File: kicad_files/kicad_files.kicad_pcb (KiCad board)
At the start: 2 copper layers, 150 x 100 mm, 68 parts, among them J1 Battery Connection, J2 Servo Connection, J3 DC Motor Connection, J4 Washout Ultrasonic Sensor Con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, J5 Water Sensor Connection, J6 Servo Connection, J7 Larvicide Level Ultrasonic Se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, Q1 FS8205A, Q2 NPN, Q3 NMOS, Q4 NMOS, Q5 NPN, Q7 NMOS, U1 BQ27441DRZR-G1A, U2 DW01A, U3 TPS61023DRLR, U4 LM311, U5 LMC555CMMX_NOPB, U6 LMC555CMMX_NOPB

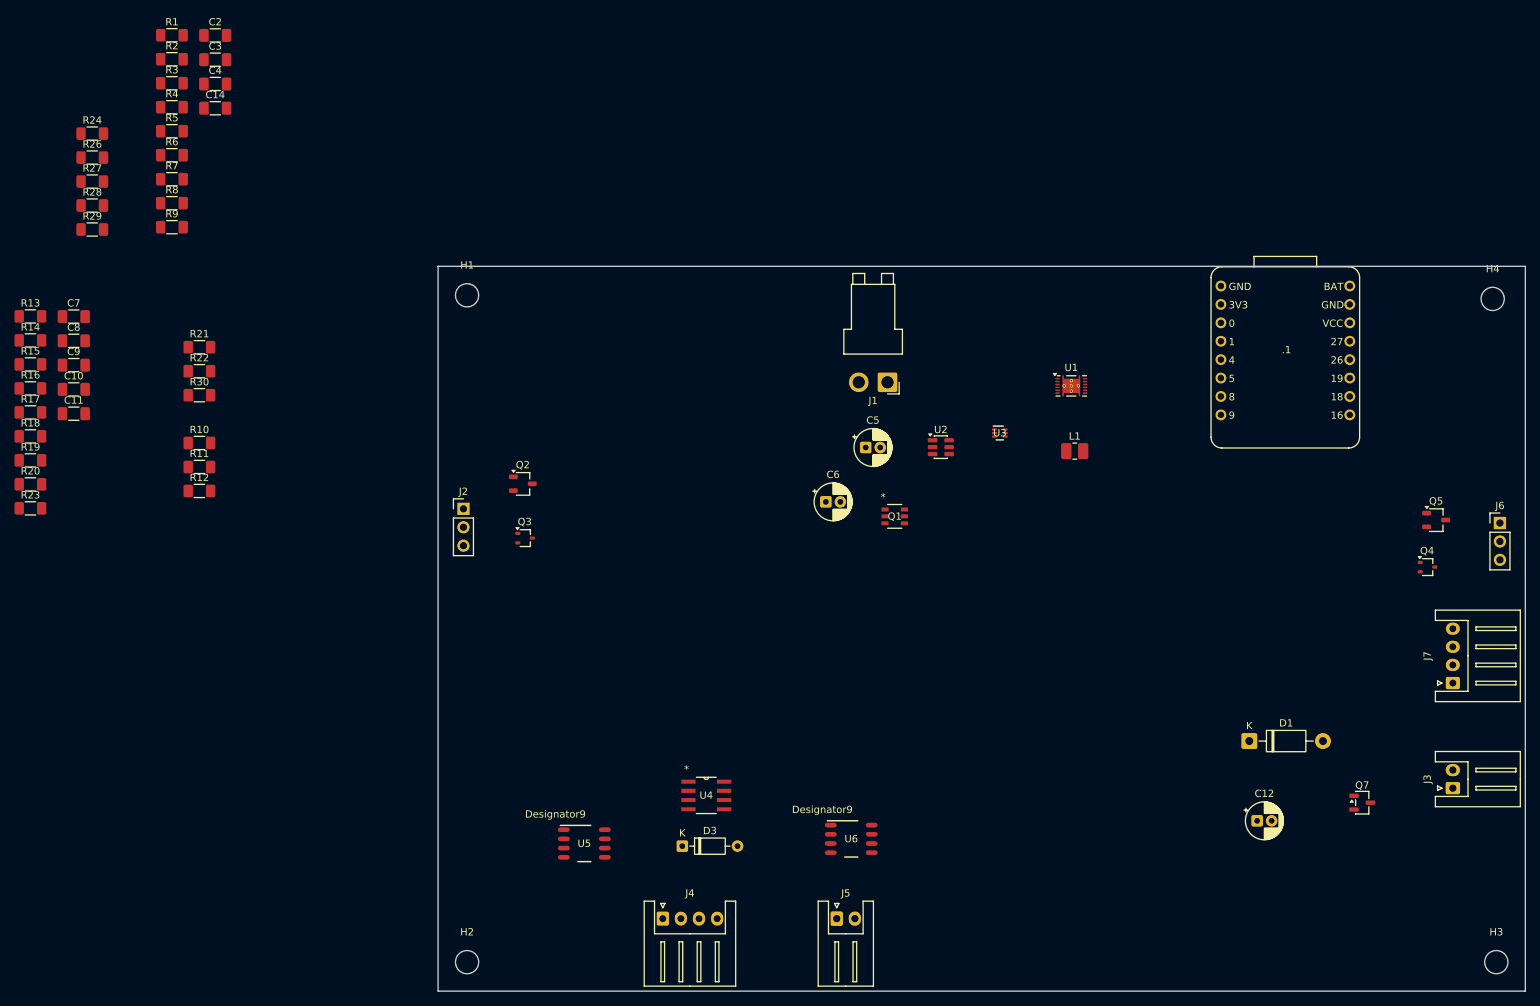
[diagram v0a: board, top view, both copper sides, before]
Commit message: Housing and Dispensing Subsystem Models
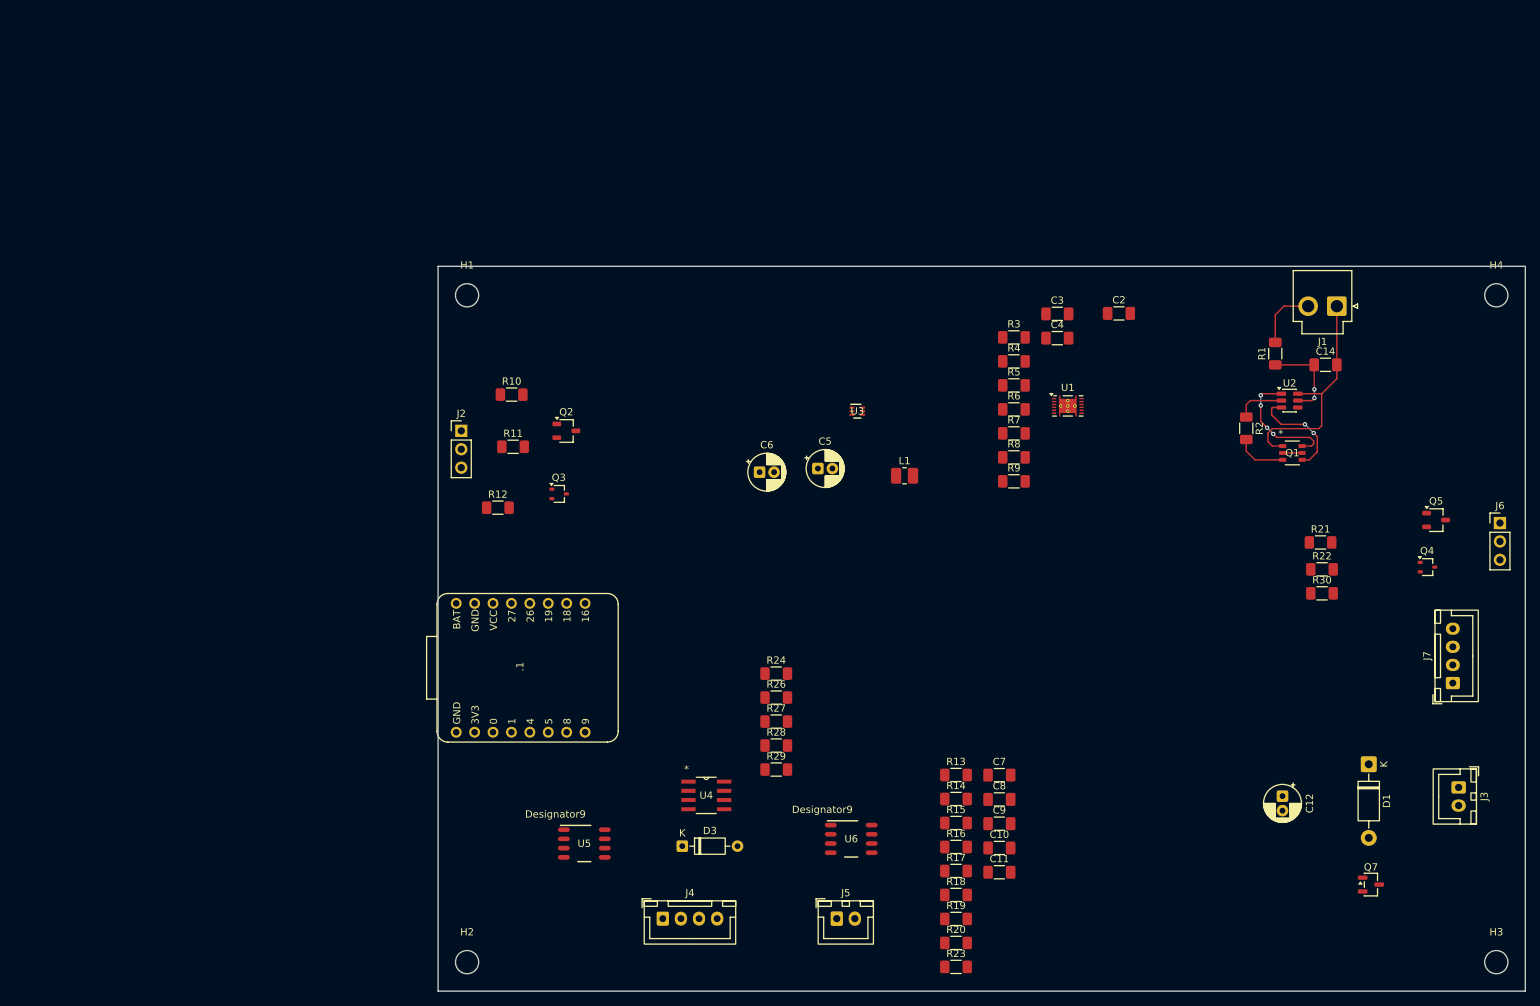
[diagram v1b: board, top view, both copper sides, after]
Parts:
- J1: footprint Connector_JST:JST_VH_B2PS-VH_1x02_P3.96mm_Horizontal -> Connector_JST:JST_VH_B2P-VH_1x02_P3.96mm_Vertical
- J3, J5: footprint Connector_JST:JST_XH_S2B-XH-A_1x02_P2.50mm_Horizontal -> Connector_JST:JST_XH_B2B-XH-A_1x02_P2.50mm_Vertical
- J4, J7: footprint Connector_JST:JST_XH_S4B-XH-A_1x04_P2.50mm_Horizontal -> Connector_JST:JST_XH_B4B-XH-A_1x04_P2.50mm_Vertical
- moved R1 158.4 mm to (215.5, 62.0), turned to 90 degrees
- moved R22 157.3 mm to (221.9, 91.8)
- moved R30 157.3 mm to (221.9, 95.1)
- moved C14 157.2 mm to (222.4, 63.6)
- moved R21 157.0 mm to (221.8, 88.1)
- moved R2 156.7 mm to (211.5, 72.3), turned to -90 degrees
- moved R13 142.5 mm to (171.5, 120.2)
- moved R14 142.5 mm to (171.5, 123.5)
- moved R15 142.5 mm to (171.5, 126.8)
- moved R16 142.5 mm to (171.5, 130.1)
- moved R17 142.5 mm to (171.5, 133.4)
- moved R18 142.5 mm to (171.5, 136.7)
- moved R19 142.5 mm to (171.5, 140.0)
- moved R20 142.5 mm to (171.5, 143.3)
- moved R23 142.5 mm to (171.5, 146.7)
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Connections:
- .1 pad 10: GND -> /MCU/larvLevelSonarEcho
- .1 pad 11: unconnected-(.1-USB_5V-Pad11) -> /MCU/uiServo
- .1 pad 12: /Dispensing Unit/MCU Motor 1 -> (no net)
- .1 pad 13: /MCU/washoutIn -> /Dispensing Unit/MCU Motor 1
- .1 pad 14: /MCU/uiServo -> unconnected-(.1-USB_5V-Pad14)
- .1 pad 15: /MCU/larvLevelSonarEcho -> GND
- .1 pad 16: /MCU/larvLevelSonarTrig -> /MCU/Bat+
- .1 pad 9: /MCU/Bat+ -> /MCU/larvLevelSonarTrig
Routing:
- net /Power Subsystem/Bat-: track 0.00 -> 32.0 mm
- net Net-(U2-OD): track 0.00 -> 17.1 mm, vias 0 -> 4
- net Net-(U2-OC): track 0.00 -> 14.5 mm, vias 0 -> 2
- net Net-(U2-VCC): track 0.00 -> 12.4 mm, vias 0 -> 2
- net /MCU/Bat+: track 0.00 -> 8.84 mm
- net GND: track 0.00 -> 7.12 mm
- net Net-(U2-CS): track 0.00 -> 6.78 mm
- net Net-(Q1-Pad2): track 0.00 -> 2.72 mm

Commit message: First pass floorplan and routing
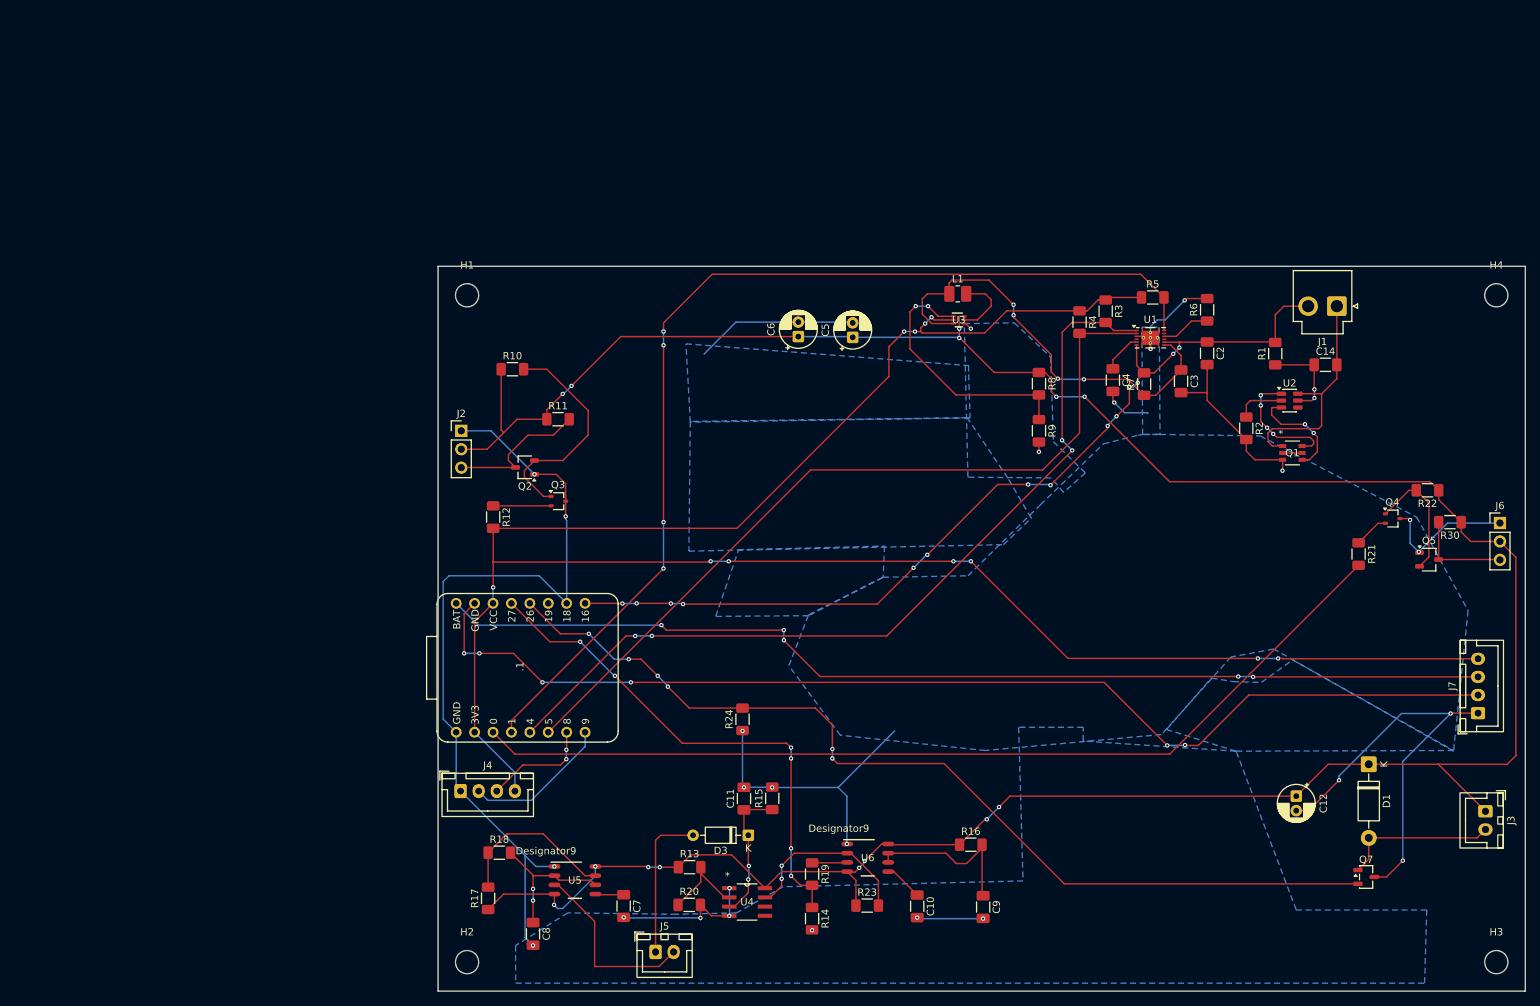
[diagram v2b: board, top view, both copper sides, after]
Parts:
- removed R26, R27: 1k, Resistor_SMD:R_1206_3216Metric_Pad1.30x1.75mm_HandSolder
- removed R28, R29: 2k, Resistor_SMD:R_1206_3216Metric_Pad1.30x1.75mm_HandSolder
- moved C8 67.0 mm to (113.1, 142.1), turned to -90 degrees
- moved R17 64.7 mm to (106.9, 137.2), turned to 90 degrees
- moved R18 63.3 mm to (108.5, 130.9)
- moved C7 54.9 mm to (125.6, 138.3), turned to -90 degrees
- moved R13 38.9 mm to (134.7, 132.9)
- moved R20 37.2 mm to (134.7, 138.1)
- moved C11 36.7 mm to (142.2, 123.4), turned to 90 degrees
- moved J4 33.0 mm to (103.1, 122.4)
- moved R6 30.0 mm to (206.1, 56.0), turned to 90 degrees
- moved L1 26.2 mm to (171.7, 53.8)
- moved R14 25.8 mm to (151.6, 140.0), turned to -90 degrees
- moved R15 25.6 mm to (146.1, 123.4), turned to 90 degrees
- moved J5 25.4 mm to (130.0, 144.6)
- moved R5 22.7 mm to (198.6, 54.3)
- moved R19 20.8 mm to (151.6, 133.8), turned to -90 degrees
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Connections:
- .1 pad 10: /MCU/larvLevelSonarEcho -> GND
- .1 pad 11: /MCU/uiServo -> unconnected-(.1-USB_5V-Pad11)
- .1 pad 12: (no net) -> /Dispensing Unit/MCU Motor 1
- .1 pad 13: /Dispensing Unit/MCU Motor 1 -> /MCU/washoutIn
- .1 pad 14: unconnected-(.1-USB_5V-Pad14) -> /MCU/3V3
- .1 pad 15: GND -> /MCU/larvLevelSonarEcho
- .1 pad 16: /MCU/Bat+ -> /MCU/larvLevelSonarTrig
- .1 pad 9: /MCU/larvLevelSonarTrig -> /MCU/Bat+
- J4 pad 2: Net-(J4-Pin_2) -> /MCU/washoutSonarEcho
- J4 pad 4: /Dispensing Unit/5V -> /MCU/3V3
- J7 pad 2: Net-(J7-Pin_2) -> /MCU/larvLevelSonarEcho
- J7 pad 4: /Dispensing Unit/5V -> /MCU/3V3
- R12 pad 2: /MCU/uiServo -> /MCU/3V3
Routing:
- net /Dispensing Unit/5V: track 0.00 -> 380.3 mm, vias 0 -> 14
- net GND: track 7.12 -> 338.5 mm, vias 0 -> 26
- net /MCU/3V3: track 0.00 -> 292.1 mm, vias 0 -> 11
- net /MCU/larvLevelSonarEcho: track 0.00 -> 155.6 mm, vias 0 -> 6
- net /MCU/larvLevelSonarTrig: track 0.00 -> 146.0 mm, vias 0 -> 5
- net /MCU/batteryLevTrigPin: track 0.00 -> 142.9 mm, vias 0 -> 4
- net /Dispensing Unit/MCU Motor 1: track 0.00 -> 133.0 mm, vias 0 -> 6
- net /Dispensing Unit/MCU PWM Dispense: track 0.00 -> 131.5 mm
- net /MCU/batteryLevDataPin: track 0.00 -> 119.1 mm, vias 0 -> 4
- net /MCU/Bat+: track 8.84 -> 127.9 mm, vias 0 -> 14
- net /MCU/batteryLevClkPin: track 0.00 -> 112.0 mm
- net /MCU/washoutIn: track 0.00 -> 71.0 mm, vias 0 -> 6
- net Net-(U1-SRN): track 0.00 -> 60.0 mm, vias 0 -> 4
- net Net-(U3-FB): track 0.00 -> 35.8 mm, vias 0 -> 2
- net Net-(Q2-B): track 0.00 -> 31.2 mm
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- added copper zone on B.Cu, net GND

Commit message: First pass revisions
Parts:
- renumbered .1 to MCU
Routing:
- net GND: track 338.5 -> 349.7 mm

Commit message: Second pass routing and floorplan
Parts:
- moved J7 135.2 mm to (111.0, 84.5), turned to 180 degrees
- moved Q4 65.7 mm to (170.2, 108.0)
- moved J6 65.2 mm to (185.2, 107.8)
- moved Q5 65.2 mm to (175.5, 112.8)
- moved R21 65.2 mm to (165.8, 112.0)
- moved R22 65.2 mm to (175.2, 103.2)
- moved R30 65.2 mm to (178.3, 107.6)
- moved C12 37.9 mm to (181.8, 132.8)
- moved Q7 37.9 mm to (191.4, 144.0)
- moved D1 37.9 mm to (191.8, 128.4)
- moved J3 37.9 mm to (207.8, 134.9)
- moved R11 36.6 mm to (147.1, 91.4)
- moved Q2 36.6 mm to (142.5, 98.0)
- moved Q3 36.6 mm to (147.1, 102.7)
- moved R10 36.6 mm to (140.8, 84.5)
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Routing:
- net GND: track 349.7 -> 197.2 mm, vias 26 -> 24
- net /MCU/larvLevelSonarEcho: track 155.6 -> 9.80 mm, vias 6 -> 0
- net /MCU/larvLevelSonarTrig: track 146.0 -> 9.81 mm, vias 5 -> 0
- net /Dispensing Unit/5V: track 380.3 -> 268.9 mm, vias 14 -> 12
- net /MCU/3V3: track 292.1 -> 181.7 mm, vias 11 -> 6
- net /Dispensing Unit/MCU PWM Dispense: track 131.5 -> 63.1 mm
- net /MCU/batteryLevTrigPin: track 142.9 -> 104.5 mm, vias 4 -> 8
- net /MCU/batteryLevDataPin: track 119.1 -> 85.0 mm, vias 4 -> 11
- net /MCU/batteryLevClkPin: track 112.0 -> 81.5 mm, vias 0 -> 11
- net /Dispensing Unit/MCU Motor 1: track 133.0 -> 107.1 mm, vias 6 -> 8
- net /MCU/Bat+: track 127.9 -> 114.3 mm, vias 14 -> 10
- net /MCU/washoutIn: track 71.0 -> 78.6 mm
- net /MCU/washoutSonarTrig: track 15.2 -> 19.3 mm, vias 2 -> 0
- net Net-(U1-SRN): track 60.0 -> 63.3 mm, vias 4 -> 0
- net /MCU/washoutSonarEcho: track 20.3 -> 23.5 mm
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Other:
- board size 150 x 100 mm -> 117.8 x 88.8 mm

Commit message: Floorplan revisions
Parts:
- moved C14 14.3 mm to (204.6, 99.1)
- moved J1 14.3 mm to (206.2, 91.0)
- moved Q1 14.3 mm to (200.1, 111.3)
- moved R1 14.3 mm to (197.7, 97.5)
- moved R2 14.3 mm to (193.7, 107.8)
- moved U2 14.3 mm to (199.7, 104.0)
- moved H1 6.50 mm to (104.0, 71.8)
- moved H4 6.50 mm to (213.8, 71.8)
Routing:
- net /MCU/Bat+: track 114.3 -> 116.4 mm
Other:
- board size 117.8 x 88.8 mm -> 117.8 x 82.2 mm

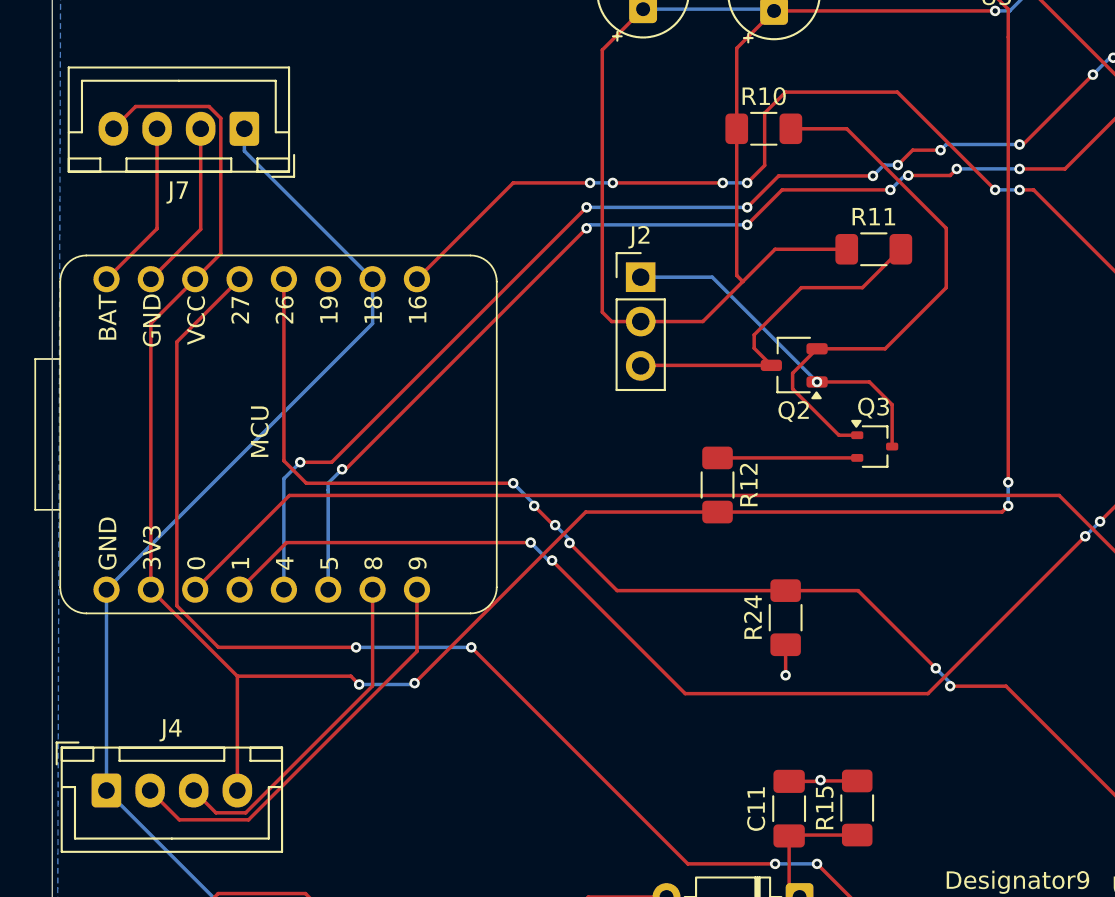
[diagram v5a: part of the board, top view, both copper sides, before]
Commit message: Schematic and Footprint error fix
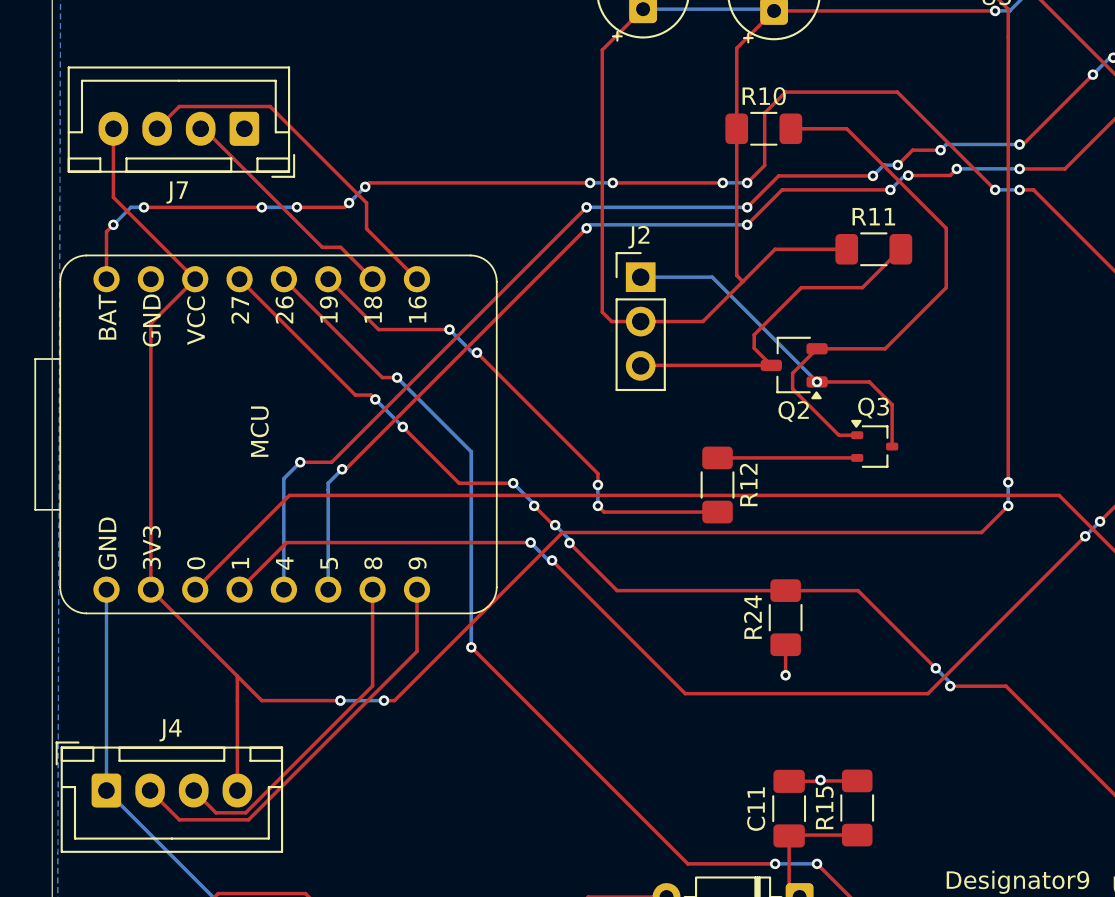
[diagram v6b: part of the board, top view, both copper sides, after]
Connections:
- MCU pad 10: GND -> /MCU/larvLevelSonarEcho
- MCU pad 11: unconnected-(.1-USB_5V-Pad11) -> /MCU/uiServo
- MCU pad 12: /Dispensing Unit/MCU Motor 1 -> /MCU/washoutIn
- MCU pad 13: /MCU/washoutIn -> /Dispensing Unit/MCU Motor 1
- MCU pad 14: /MCU/3V3 -> unconnected-(.1-USB_5V-Pad14)
- MCU pad 15: /MCU/larvLevelSonarEcho -> GND
- MCU pad 16: /MCU/larvLevelSonarTrig -> /MCU/Bat+
- MCU pad 9: /MCU/Bat+ -> /MCU/larvLevelSonarTrig
- R12 pad 2: /MCU/3V3 -> /MCU/uiServo
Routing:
- net GND: track 196.9 -> 161.2 mm
- net /MCU/uiServo: track 0.00 -> 28.9 mm, vias 0 -> 4
- net /MCU/Bat+: track 116.4 -> 135.8 mm, vias 10 -> 16
- net /MCU/washoutIn: track 78.6 -> 66.6 mm
- net /MCU/larvLevelSonarTrig: track 9.81 -> 20.4 mm
- net /MCU/3V3: track 181.7 -> 176.2 mm
- net /MCU/larvLevelSonarEcho: track 9.80 -> 13.4 mm
- net /Dispensing Unit/MCU Motor 1: track 107.1 -> 103.5 mm, vias 8 -> 10
